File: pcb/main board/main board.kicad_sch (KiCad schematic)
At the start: 44 parts, among them J10 12V Battery, J11 BAU, J12 Servo 4 Conn, J13 Servo 1 Conn, J14 Servo 2 Conn, J15 Servo 3 Conn, J16 Servo 5 Conn, J17 Servo 6 Conn, J18 Servo 7 Conn, J19 Servo 8 Conn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

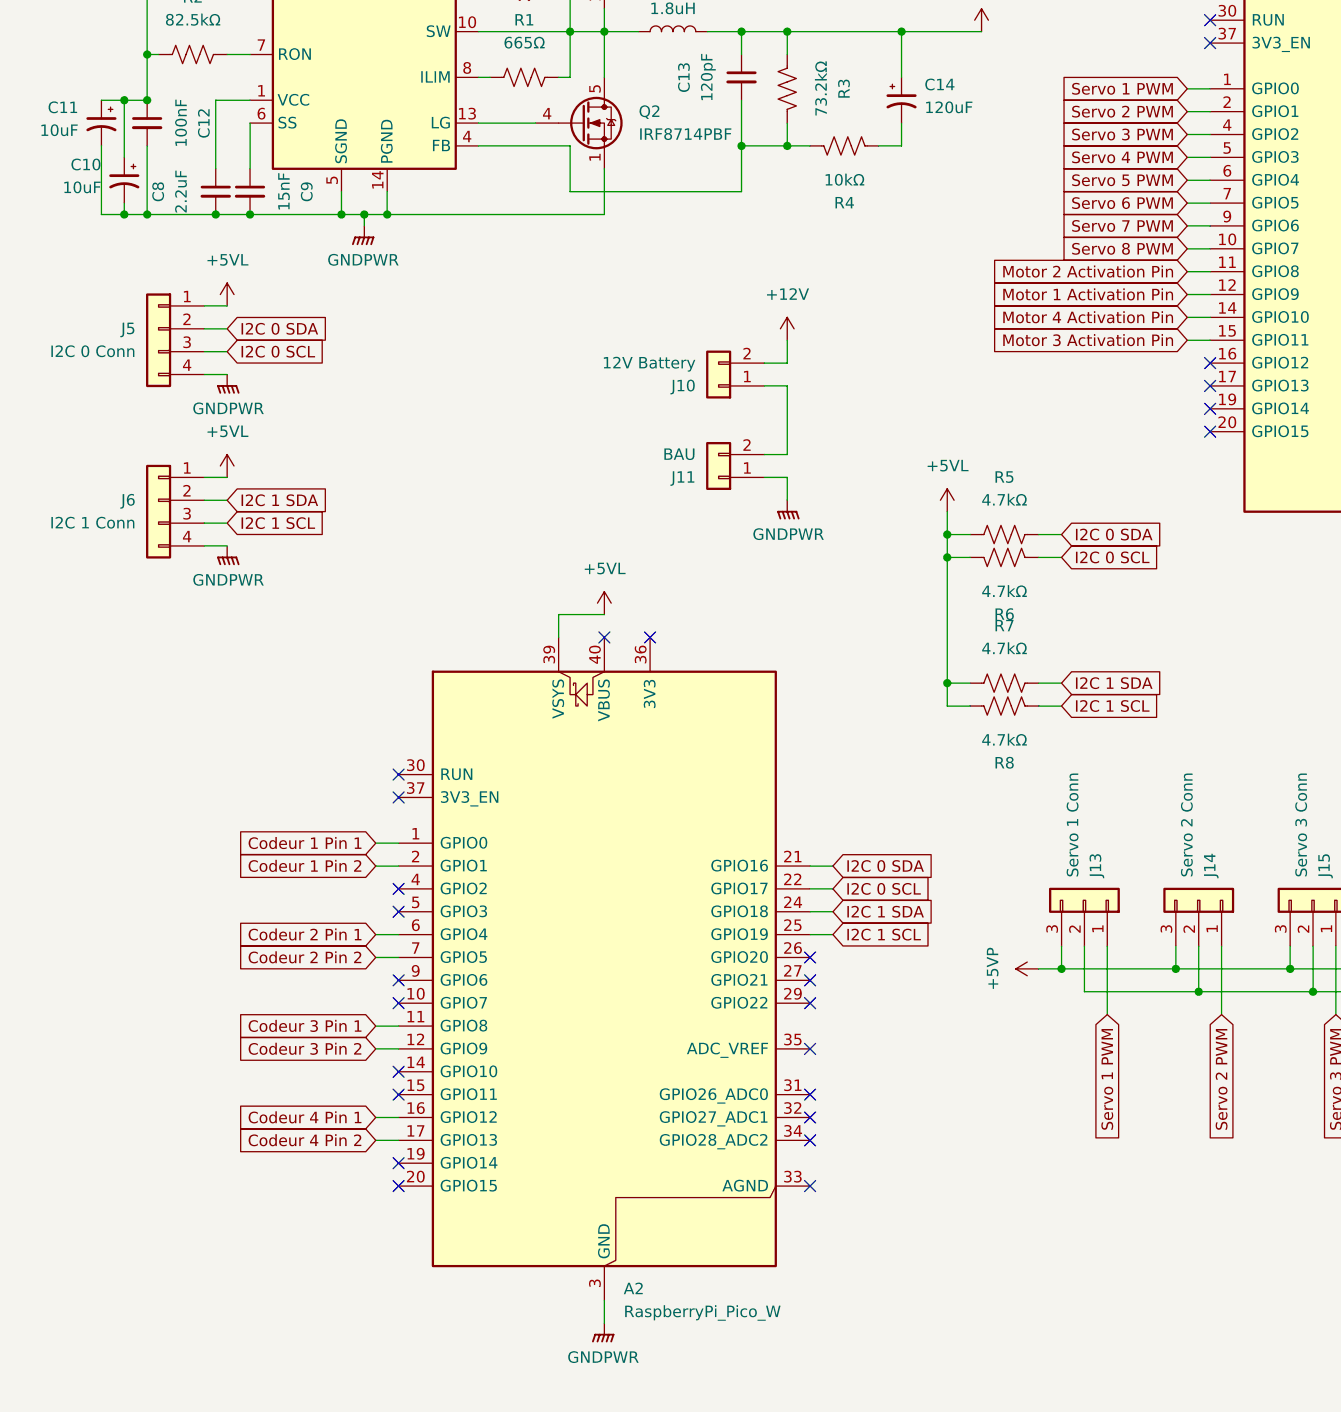
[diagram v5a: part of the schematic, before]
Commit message: Finished adding holes and connectors
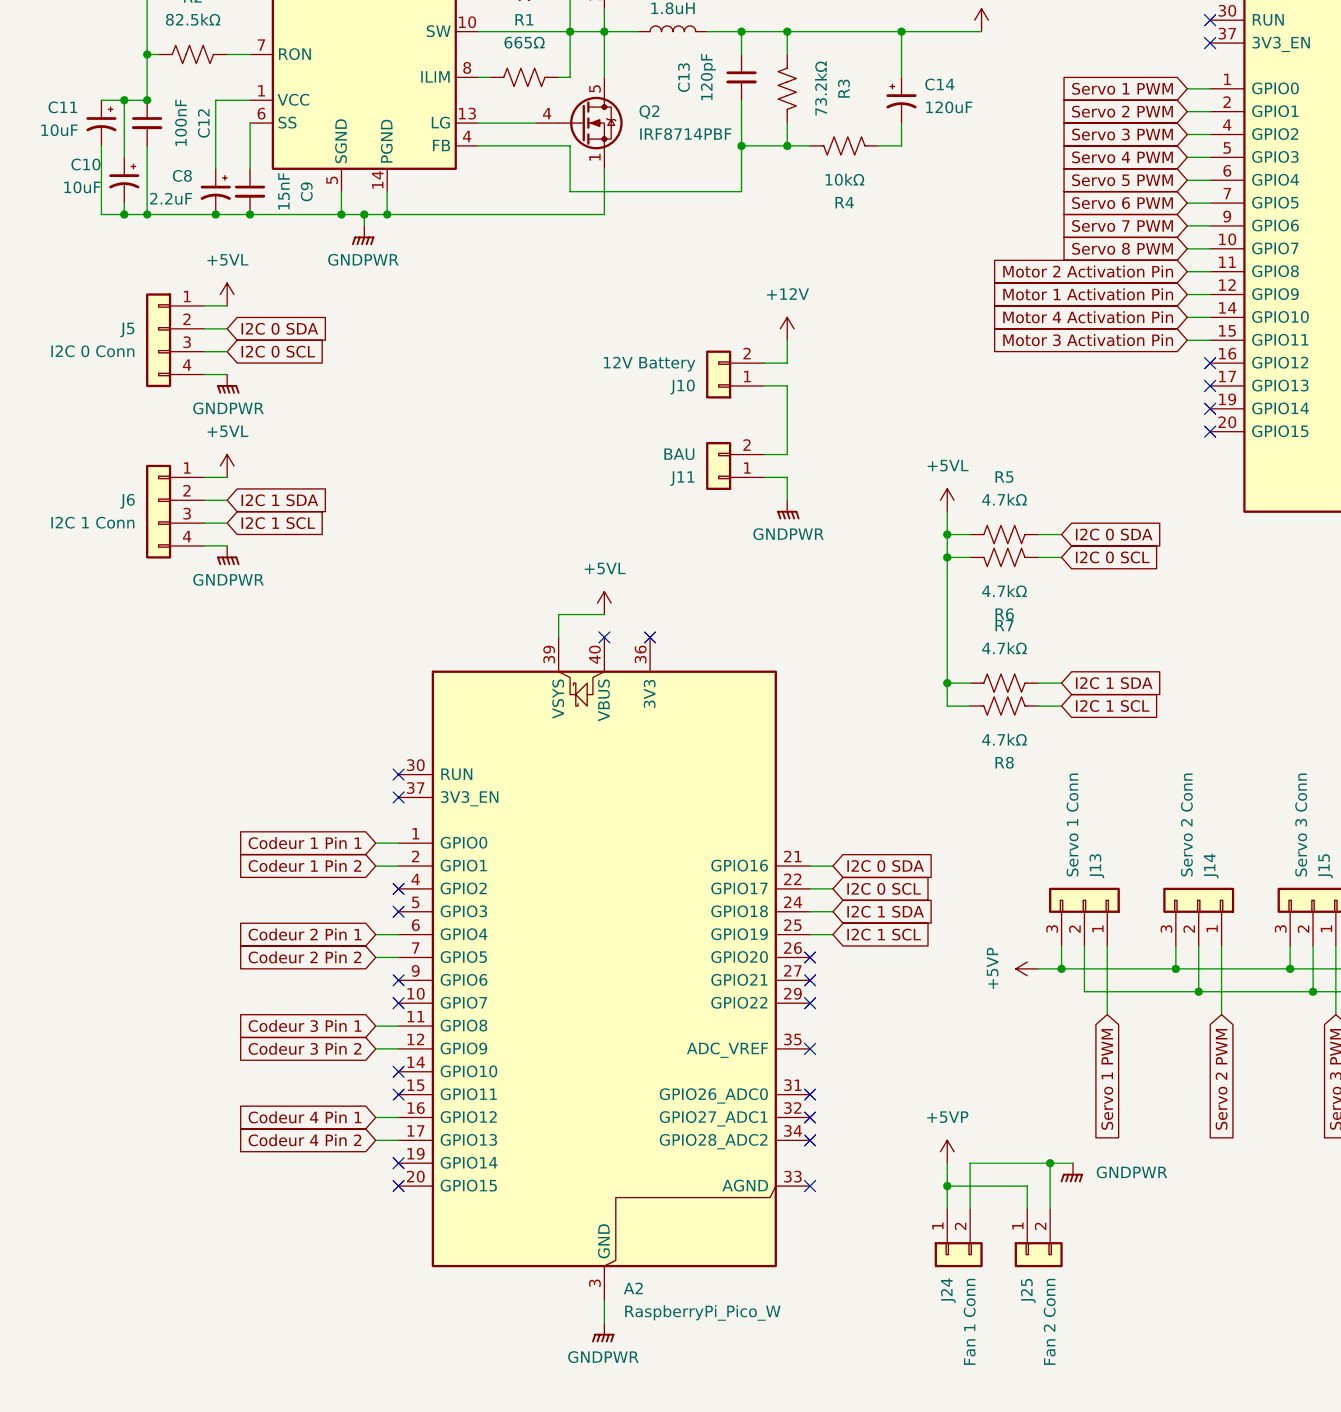
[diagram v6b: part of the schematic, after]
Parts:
- removed C8: 2.2uF, Capacitor_THT:C_Radial_D6.3mm_H5.0mm_P2.50mm, symbol Device:C_Small
- added C8: 2.2uF, Capacitor_THT:CP_Radial_D5.0mm_P2.00mm, symbol Device:C_Polarized_Small_US
- added J24: Fan 1 Conn, Connector_Molex:Molex_KK-254_AE-6410-02A_1x02_P2.54mm_Vertical, symbol Connector_Generic:Conn_01x02
- added J25: Fan 2 Conn, Connector_Molex:Molex_KK-254_AE-6410-02A_1x02_P2.54mm_Vertical, symbol Connector_Generic:Conn_01x02
- H1, H2, H3, H4: footprint MountingHole:MountingHole_3.2mm_M3_Pad -> MountingHole:MountingHole_4mm_Pad
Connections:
- net +5VP: now also J24.1 (Pin_1), J25.1 (Pin_1)
- net GNDPWR: now also C8.2, J24.2 (Pin_2), J25.2 (Pin_2)
- net at U6.1 (VCC): now also C8.1

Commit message: Updated PCB and corrected errors
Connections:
- net GNDPWR: now also C14.2, R4.1
- net at C13.2, R3.1, U6.4 (FB): now also R4.2; no longer R4.1
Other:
- moved on the sheet: C14, R3, R4
